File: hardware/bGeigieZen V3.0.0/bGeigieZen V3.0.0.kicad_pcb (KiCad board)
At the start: 2 copper layers, 129.4 x 64.6 mm, 28 parts, among them J1 M5 2x15 pin, J10 QI GND, J11 QI charger Plus, J2 Geiger, J3 GPS, J4 Geiger 2, J5 Extra support header, J6 Grove, J7 Grove, J8 QI charger ground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

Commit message: Updated, cleaned out old files
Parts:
- removed C1: 47uF, bGeigieZen:C025-024X044
- removed H1, H10, H2, H3, H5, H7, H8, H9: MountingHole_Pad, MountingHole:MountingHole_3.2mm_M3
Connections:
- J1 pad 5: /Reset -> unconnected-(J1-Pin_5-Pad5)
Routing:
- net /Reset: track 87.7 -> 0.00 mm, vias 2 -> 0
- net /SCL: track 83.5 -> 67.2 mm, vias 1 -> 0
- net /SDA: track 61.6 -> 51.6 mm
- net 3.3V: track 140.5 -> 136.8 mm
- net /GIO2 on Core and GIO32 on Core-2: track 109.1 -> 111.8 mm, vias 0 -> 2
- net Net-(BT1--): track 61.3 -> 58.9 mm
- net GND: track 0.00 -> 1.26 mm, vias 2 -> 1
- net /VBATT: track 65.7 -> 66.3 mm
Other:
- board text removed: "+"
- board text removed: "-"

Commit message: Updated V3.0.0 board and added Draw.io file
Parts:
- removed 1850 LABEL: LOGO, bGeigieRaku_M5_1015:18650 map
- J1: footprint Connector_PinHeader_2.54mm:PinHeader_2x15_P2.54mm_Vertical_SMD -> Connector_PinHeader_2.54mm:PinHeader_2x15_P2.54mm_Vertical
- J2: value Geiger -> Geiger IRover
- J4: value Geiger 2 -> Geiger Safepulse
- moved J1 18.0 mm to (141.5, 116.4)
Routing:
- net /GIO2 on Core and GIO32 on Core-2: track 111.8 -> 138.2 mm, vias 2 -> 1
- net /TX2: track 42.1 -> 51.2 mm, vias 1 -> 0
- net /SCL: track 67.2 -> 69.5 mm
- net 3.3V: track 136.8 -> 138.9 mm
- net /BAT: track 94.6 -> 96.0 mm
- net /SDA: track 51.6 -> 52.8 mm
- net /RX2: track 40.8 -> 41.9 mm
- net Net-(BT1--): track 58.9 -> 59.6 mm

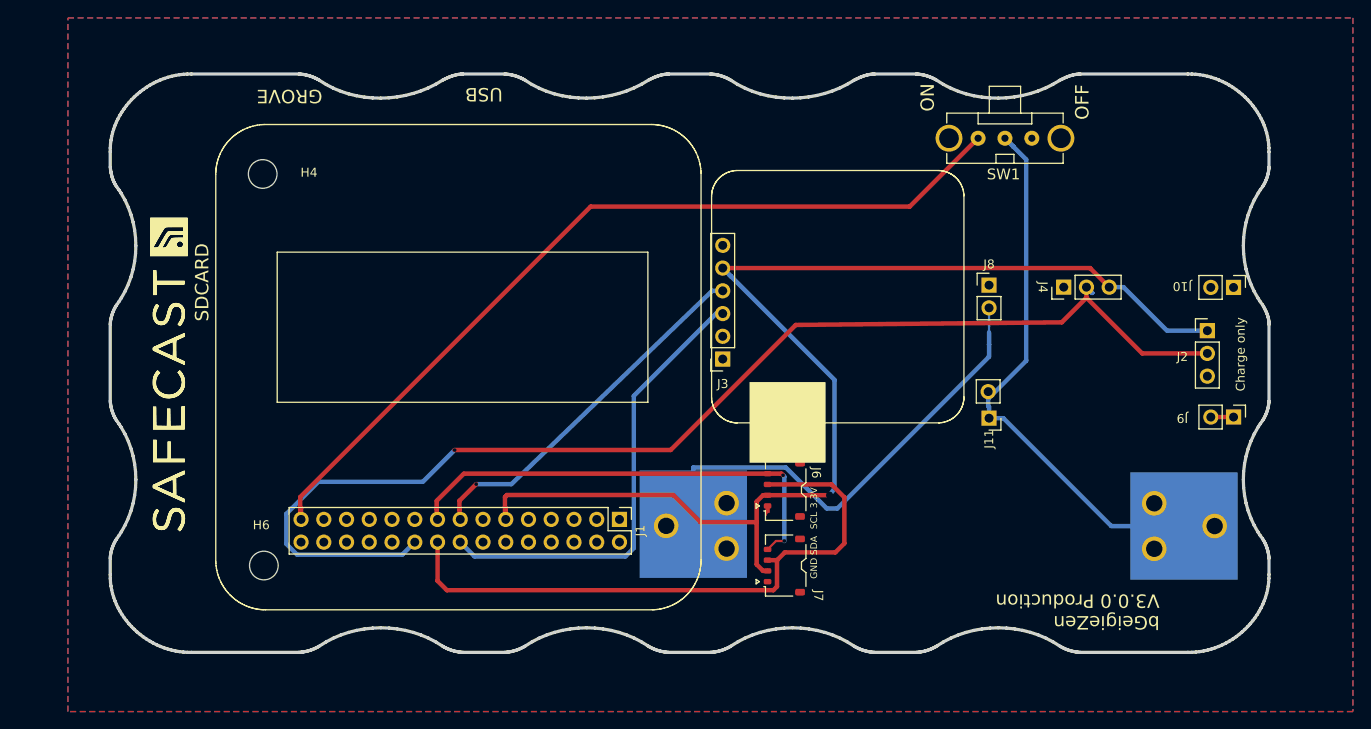
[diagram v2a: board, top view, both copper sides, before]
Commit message: Added draw.io and updated V3.0.0 board
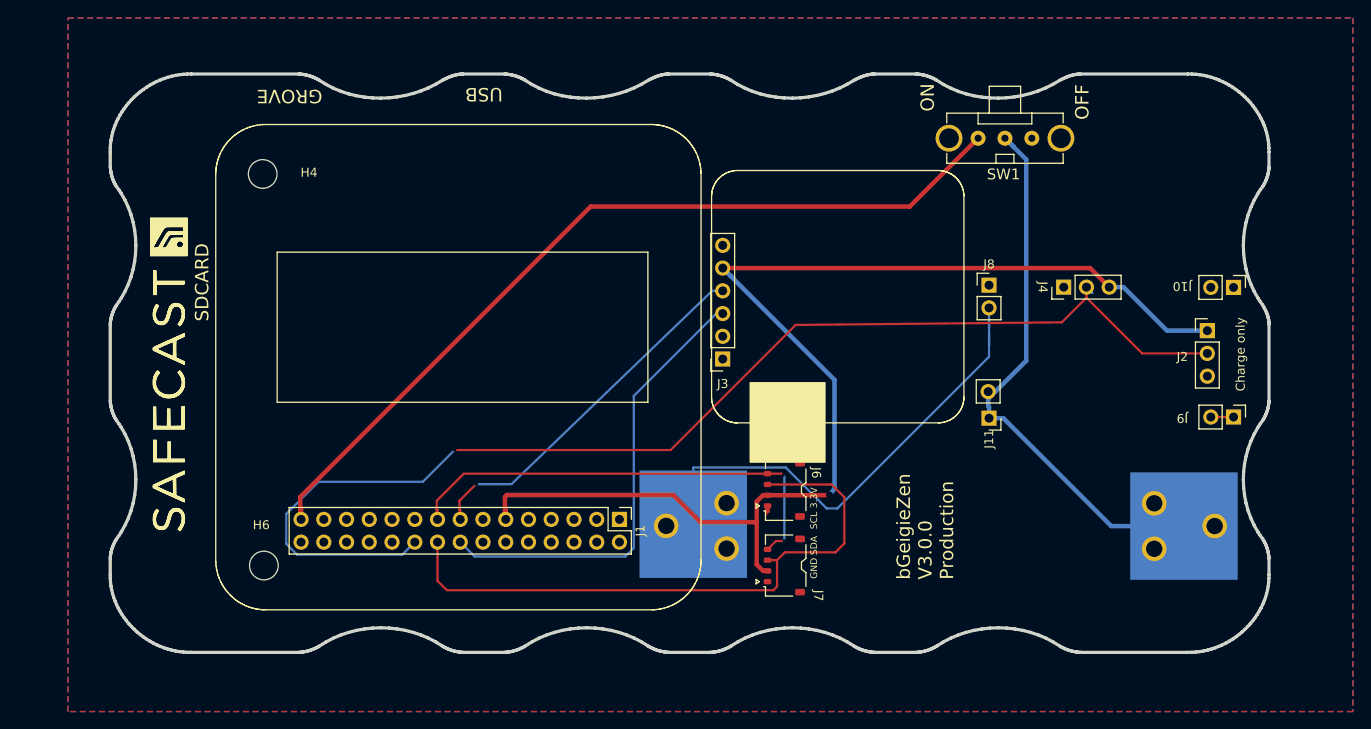
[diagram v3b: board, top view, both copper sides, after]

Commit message: Updated board V3.0.0. removed I2C connectors.
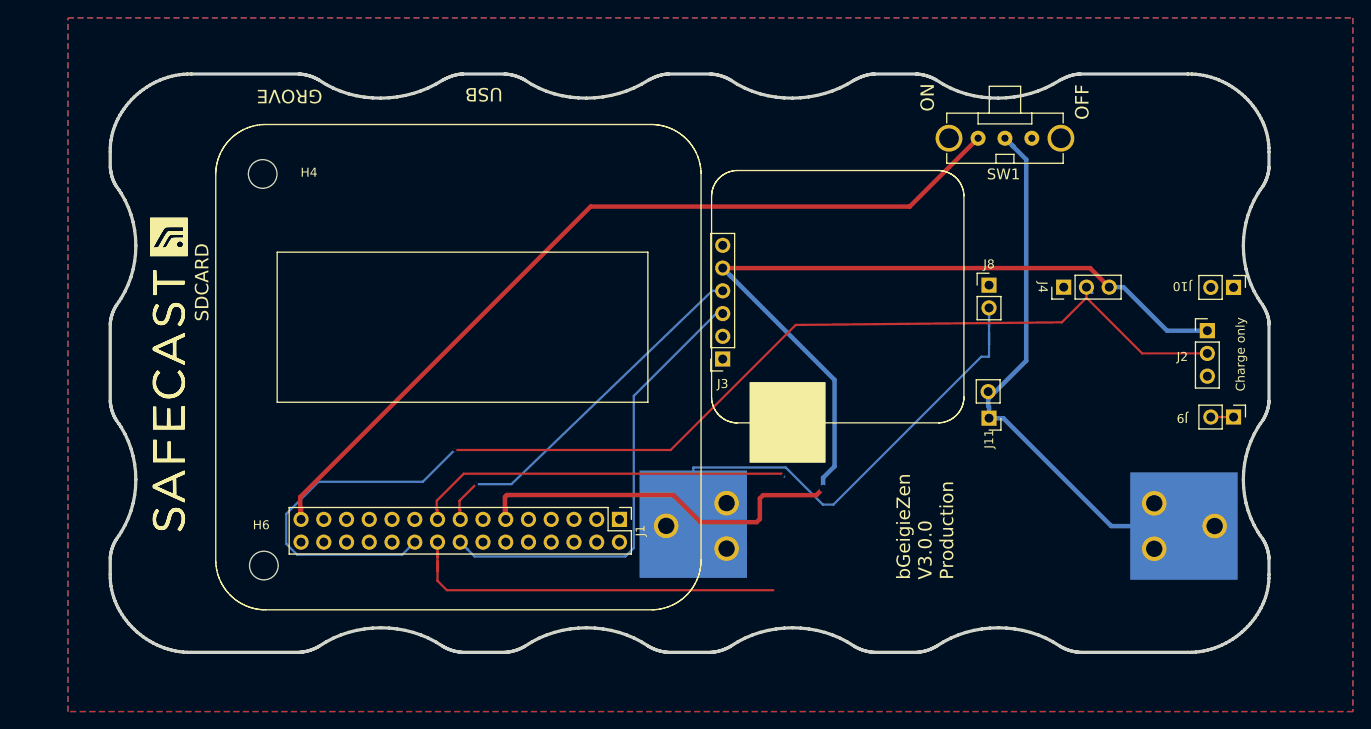
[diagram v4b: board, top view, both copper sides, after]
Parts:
- removed J6, J7: Grove, Connector_JST:JST_ACH_BM04B-ACHSS-A-GAN-ETF_1x04-1MP_P1.20mm_Vertical
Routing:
- net /SCL: track 69.5 -> 43.9 mm
- net /SDA: track 52.8 -> 43.6 mm, vias 2 -> 1
- net 3.3V: track 138.9 -> 131.8 mm
- net GND: track 1.26 -> 0.00 mm, vias 1 -> 0
- net /TX2: track 51.2 -> 52.0 mm
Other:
- board text removed: "3.3V"
- board text removed: "GND"
- board text removed: "SCL"
- board text removed: "SDA"

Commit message: added grove connector for motion sensor
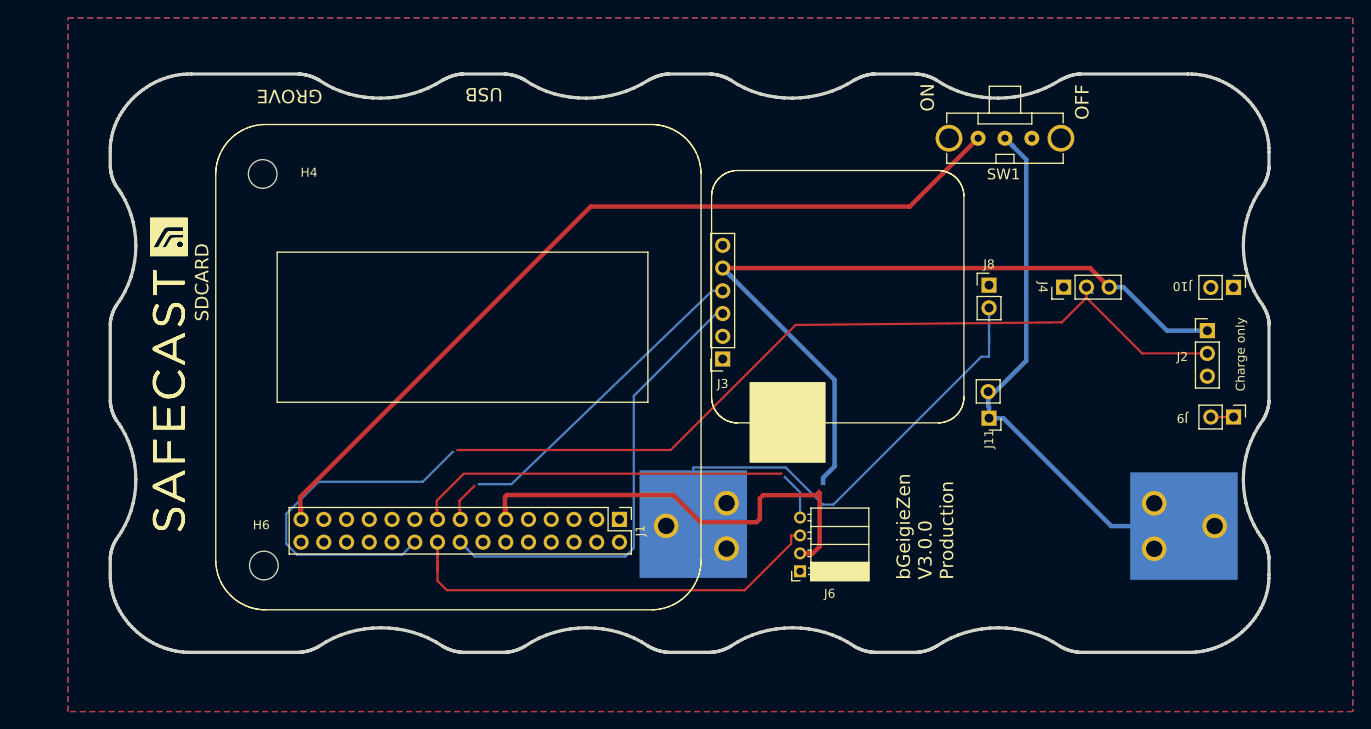
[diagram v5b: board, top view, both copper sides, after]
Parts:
- added J6: Grove, Connector_PinSocket_2.00mm:PinSocket_1x04_P2.00mm_Horizontal, F.Cu at (161.6, 122.2)
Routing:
- net 3.3V: track 131.8 -> 140.5 mm
- net /SCL: track 43.9 -> 50.5 mm
- net /SDA: track 43.6 -> 49.1 mm
